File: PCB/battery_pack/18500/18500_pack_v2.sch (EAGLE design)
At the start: 7 parts, among them P1 39-30-02, P2 B10B-PH-K, P3 B10B-PH-K, X1 5566-2

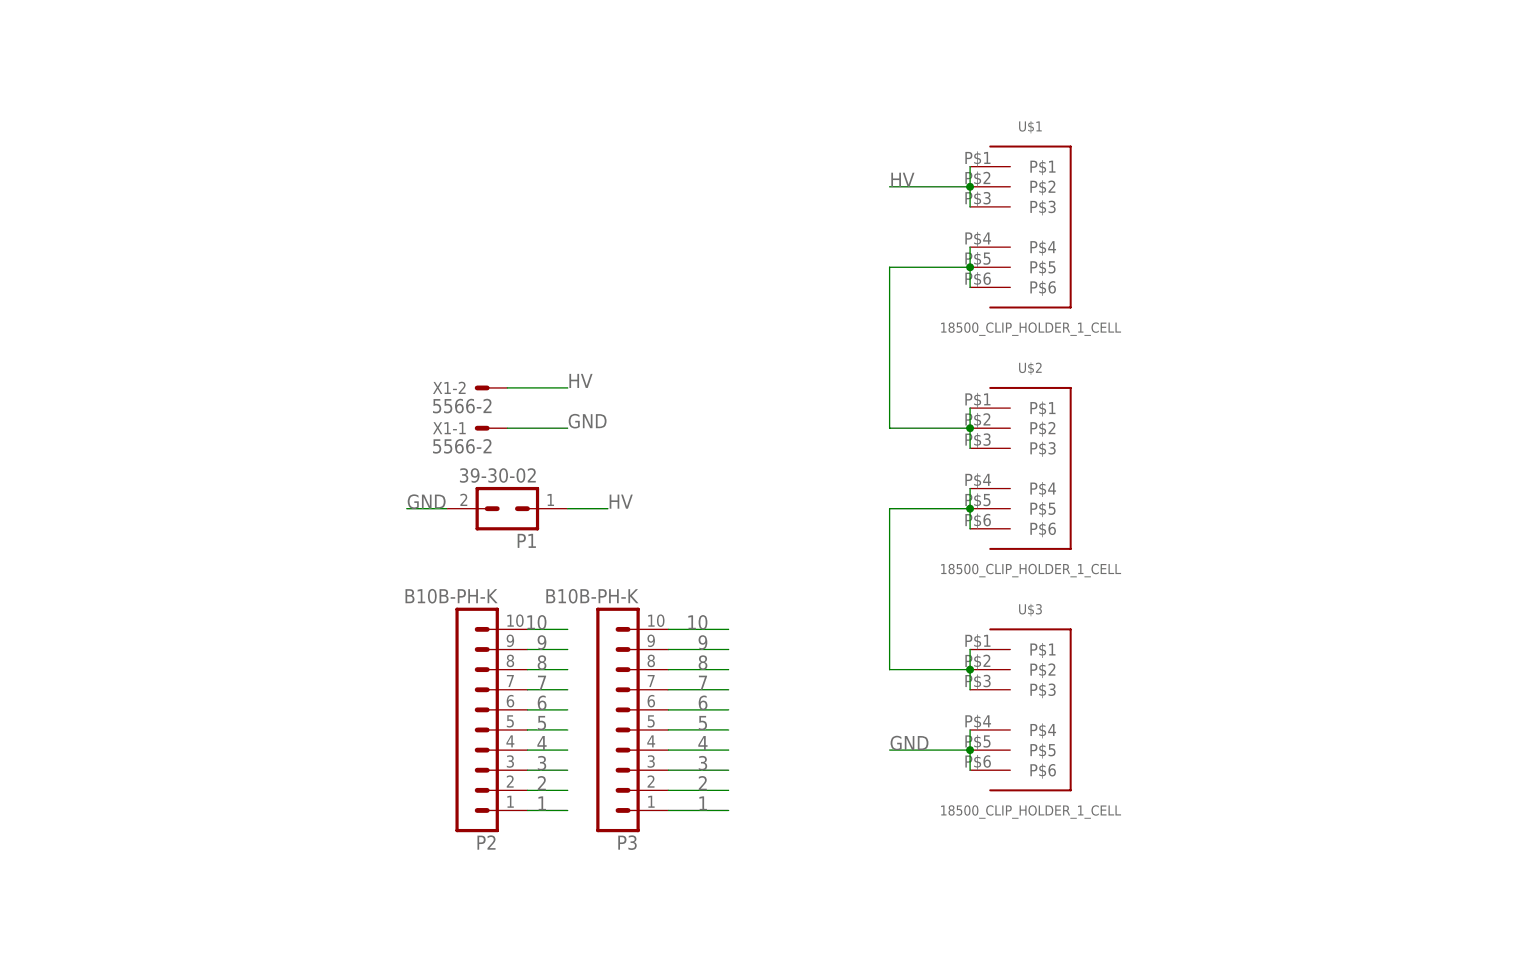
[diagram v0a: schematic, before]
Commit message: added parts_list, gerbers, and images for the 18500 pack PCB
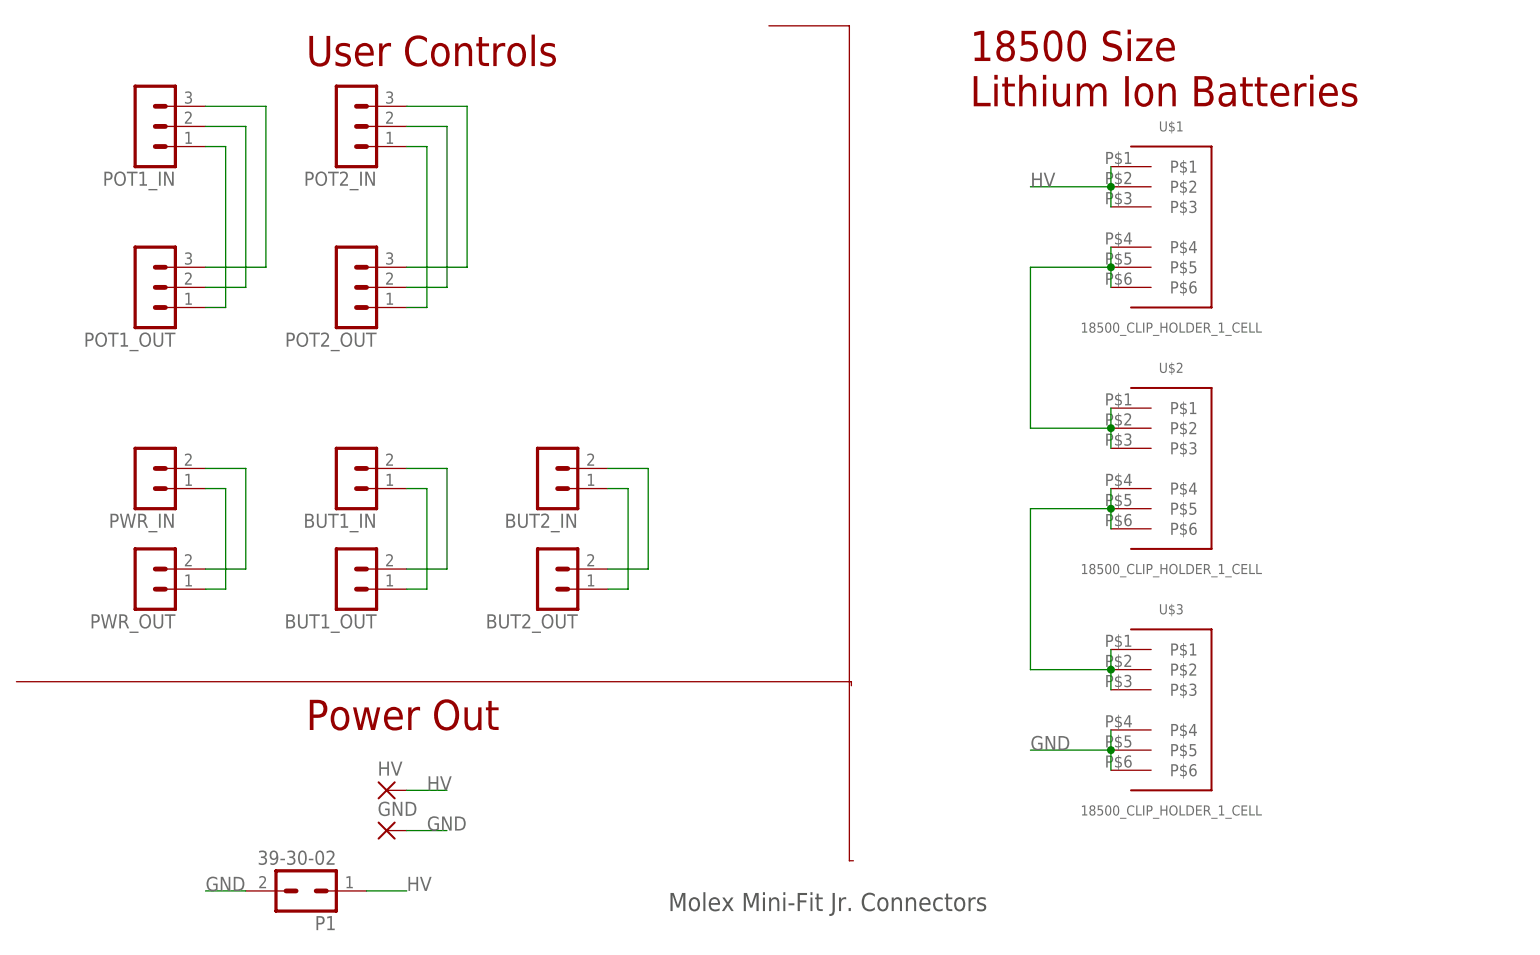
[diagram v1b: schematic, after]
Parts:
- removed P2, P3: B10B-PH-K, con-jst-ph:B10B-PH-K
- removed X1: 5566-2, con-molex:5566-2
- added BUT1_IN, BUT1_OUT, BUT2_IN, BUT2_OUT, PWR_IN, PWR_OUT: B2B-PH-K, con-jst-ph:B2B-PH-K
- added GND, HV: (no value), wirepad:2,54/1,1
- added POT1_IN, POT1_OUT, POT2_IN, POT2_OUT: B3B-PH-K, con-jst-ph:B3B-PH-K
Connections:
- removed net 1: P2.1, P3.1
- removed net 10: P2.10, P3.10
- removed net 2: P2.2, P3.2
- removed net 3: P2.3, P3.3
- removed net 4: P2.4, P3.4
- removed net 5: P2.5, P3.5
- removed net 6: P2.6, P3.6
- removed net 7: P2.7, P3.7
- removed net 8: P2.8, P3.8
- removed net 9: P2.9, P3.9
- new net N$10: POT1_IN.2, POT1_OUT.2
- new net N$11: POT1_IN.3, POT1_OUT.3
- new net N$12: POT2_IN.1, POT2_OUT.1
- new net N$13: POT2_IN.2, POT2_OUT.2
- new net N$14: POT2_IN.3, POT2_OUT.3
- new net N$3: PWR_IN.2, PWR_OUT.2
- new net N$4: PWR_IN.1, PWR_OUT.1
- new net N$5: BUT1_IN.2, BUT1_OUT.2
- new net N$6: BUT1_IN.1, BUT1_OUT.1
- new net N$7: BUT2_IN.2, BUT2_OUT.2
- new net N$8: BUT2_IN.1, BUT2_OUT.1
- new net N$9: POT1_IN.1, POT1_OUT.1
- net GND: now also GND.P; no longer X1-1.S
- net HV: now also HV.P; no longer X1-2.S
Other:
- note added: "18500 Size Lithium Ion Batteries"
- note added: "Molex Mini-Fit Jr. Connectors"
- note added: "Power Out"
- note added: "User Controls"
- moved on the sheet: P1, U$1, U$2, U$3
